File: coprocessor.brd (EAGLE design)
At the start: 27.9 x 64.8 mm, 52 parts, among them IC1 MEGA32U2, U1 TPS61090RSAR, U3 V_REG_LDOSMD2, U4 AZV321

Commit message: Added some aesthetics
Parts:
- FRAME2: value FRAME-LETTER -> Matthew Carlson
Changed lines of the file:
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@@
 </plain>
 <attributes>
+<attribute name="DESIGNER" value="Matthew Carlson"/>
 </attributes>
 <variantdefs>
@@
 <element name="LED2" library="adafruit" package="CHIPLED_0603" value="CHG" x="31.75" y="43.18"/>
 <element name="THERM" library="SparkFun-Resistors" package="0603-RES" value="16k" x="15.24" y="2.54"/>
-<element name="FRAME2" library="SparkFun-Aesthetics" package="CREATIVE_COMMONS" value="FRAME-LETTER" x="17.78" y="-10.16"/>
+<element name="FRAME2" library="SparkFun-Aesthetics" package="CREATIVE_COMMONS" value="Matthew Carlson" x="17.78" y="-10.16"/>
 <element name="U$4" library="custom" package="LOGO_1INCH" value="" x="35.56" y="2.54" rot="R90"/>
 </elements>

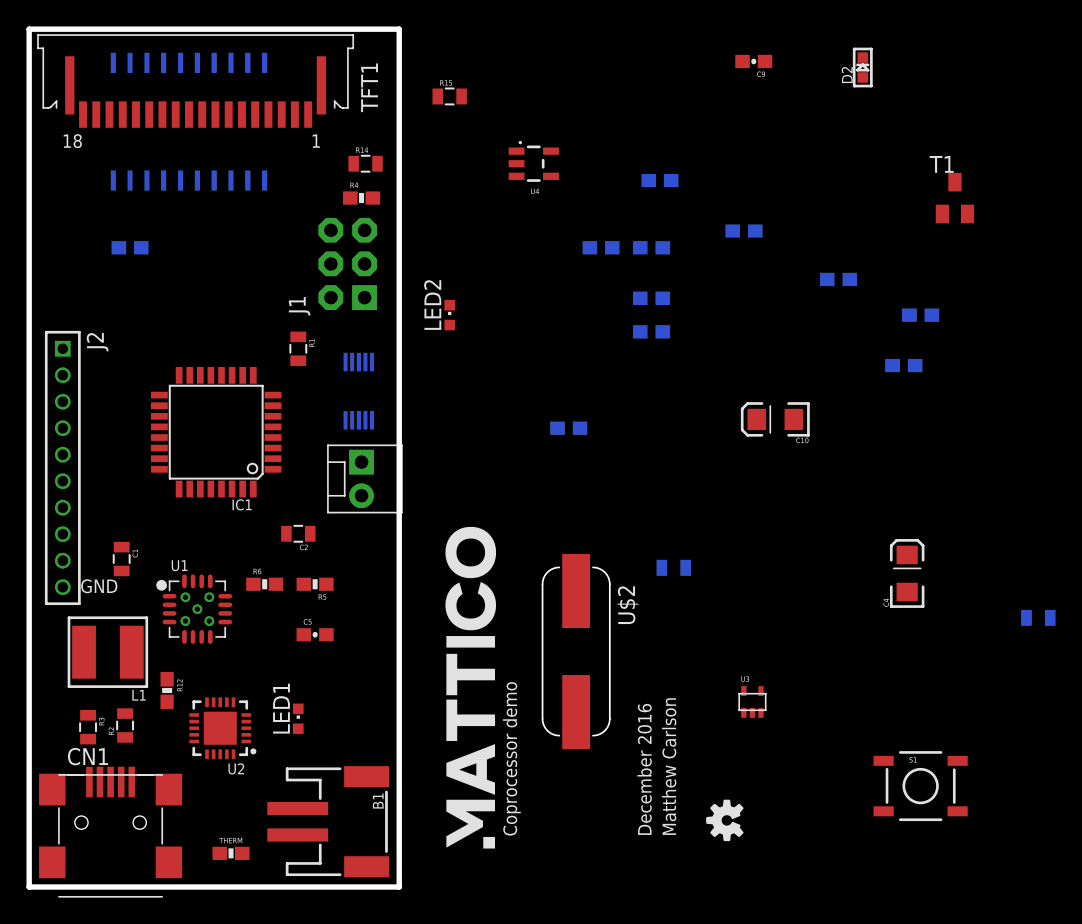
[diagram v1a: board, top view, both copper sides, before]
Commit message: final schematic for revision 2
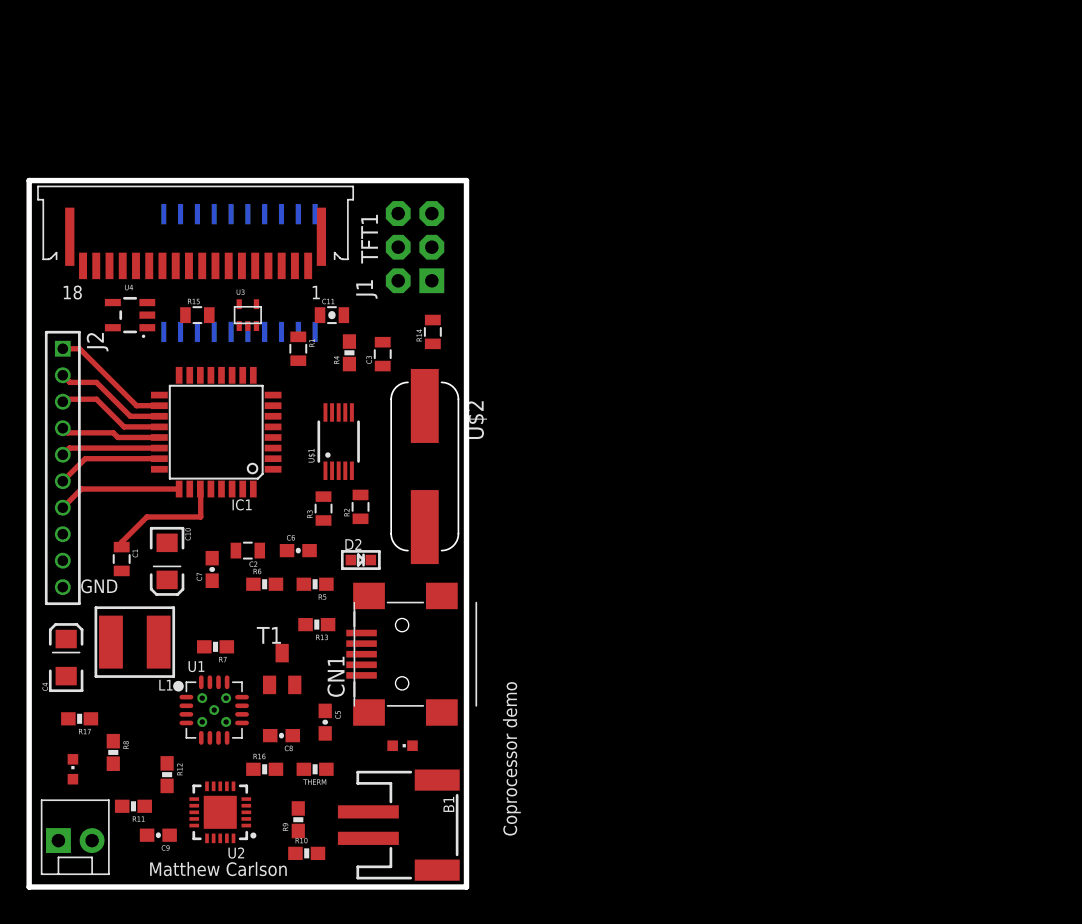
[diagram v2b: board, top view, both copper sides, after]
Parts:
- removed FRAME2: Matthew Carlson, SparkFun-Aesthetics:CREATIVE_COMMONS
- removed S1: RESET, SparkFun-Electromechanical:TACTILE-SWITCH-SMD
- moved C9 73.7 mm to (9.75, 3.91)
- moved R17 70.4 mm to (3.81, 12.7), flipped to the top, turned to 180 degrees
- moved C4 63.8 mm to (2.79, 17.3)
- moved T1 62.0 mm to (19.1, 16.5)
- moved C11 58.0 mm to (22.9, 43.2), flipped to the top
- moved R10 57.4 mm to (21.0, 2.54), flipped to the top
- moved R16 57.1 mm to (17.8, 8.89), flipped to the top
- moved R8 53.2 mm to (6.35, 10.2), flipped to the top, turned to 270 degrees
- moved D2 53.1 mm to (25.0, 24.7), turned to 270 degrees
- moved R11 53.0 mm to (7.87, 6.10), flipped to the top
- moved C7 52.1 mm to (13.8, 24.0), flipped to the top, turned to 90 degrees
- moved R9 48.9 mm to (20.3, 5.08), flipped to the top, turned to 90 degrees
- moved U3 48.0 mm to (16.5, 43.2)
- moved C10 47.2 mm to (10.4, 24.6), turned to 270 degrees
- moved C8 46.2 mm to (19.1, 11.4), flipped to the top, turned to 180 degrees
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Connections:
- new net MCU_CS: IC1.9, U$3.P$2
- new net MCU_MISO: IC1.17
- new net MCU_MOSI: IC1.16, U$3.P$6
- new net MCU_RS: IC1.8, U$3.P$8
- new net MCU_SCK: IC1.15, U$3.P$4
- new net N$28: IC1.22, J2.5
- new net N$29: IC1.23, J2.6
- new net N$30: IC1.25, J2.7
- net GND: now also J2.10; no longer S1.1
- net MISO: no longer IC1.17
- net MOSI: no longer IC1.16
- net N$25: now also IC1.19, J2.2; no longer U$3.P$4
- net N$26: now also IC1.20, J2.3; no longer U$3.P$6
- net N$27: now also IC1.21, J2.4; no longer U$3.P$8
- net N$5: now also IC1.18, J2.1; no longer U$3.P$2
- net RESET: now also J2.8; no longer S1.3
- net SCK: no longer IC1.15
- net TFT_CS: no longer IC1.9
- net TFT_RS: no longer IC1.8
- net VCC: now also J2.9
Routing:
- net N$30: track 0.00 -> 9.37 mm
- net N$7: track 0.00 -> 9.24 mm
- net N$5: track 0.00 -> 9.07 mm
- net N$25: track 0.00 -> 8.57 mm
- net N$26: track 0.00 -> 8.23 mm
- net N$29: track 0.00 -> 7.99 mm
- net N$27: track 0.00 -> 7.58 mm
- net N$28: track 0.00 -> 7.50 mm
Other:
- board size 27.9 x 64.8 mm -> 33 x 53.3 mm
- board text added: "January 2017"
- board text removed: "December 2016"

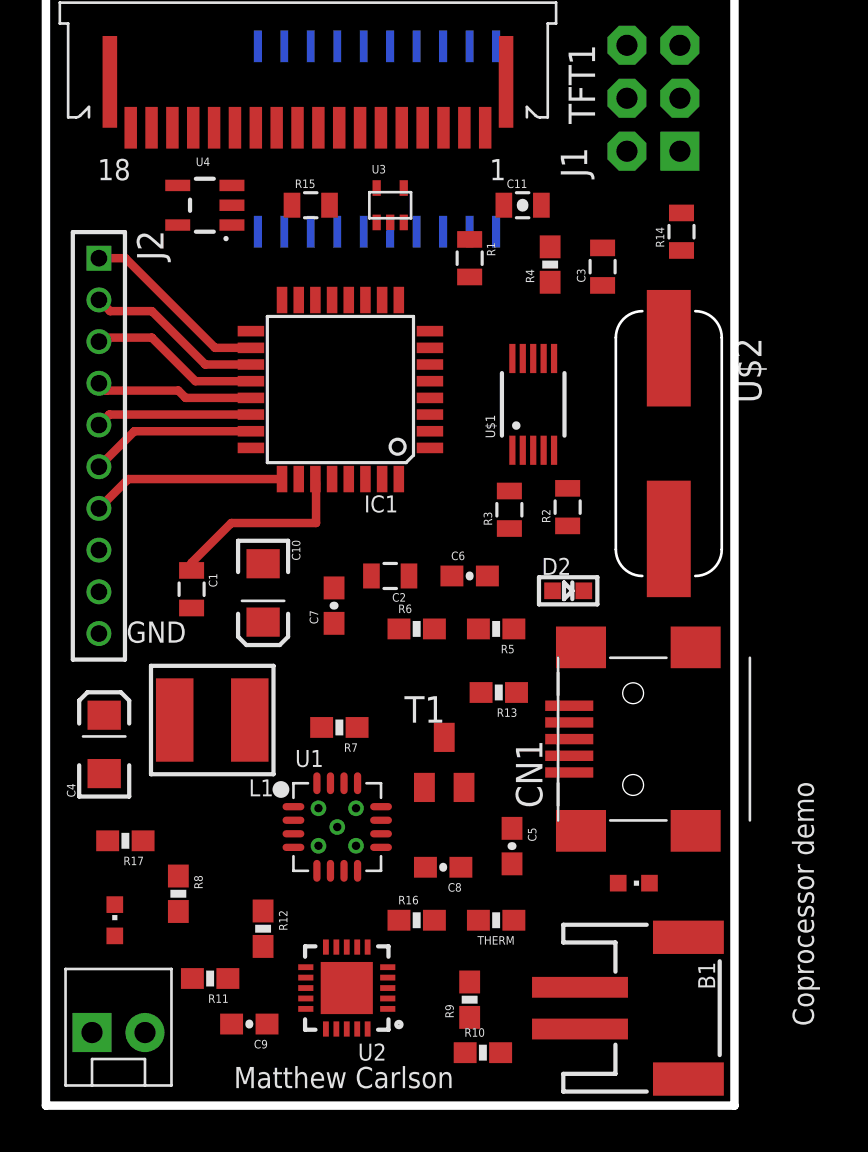
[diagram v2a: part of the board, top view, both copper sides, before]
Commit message: fixed a minor bug on the Bus switch PB2->PC2
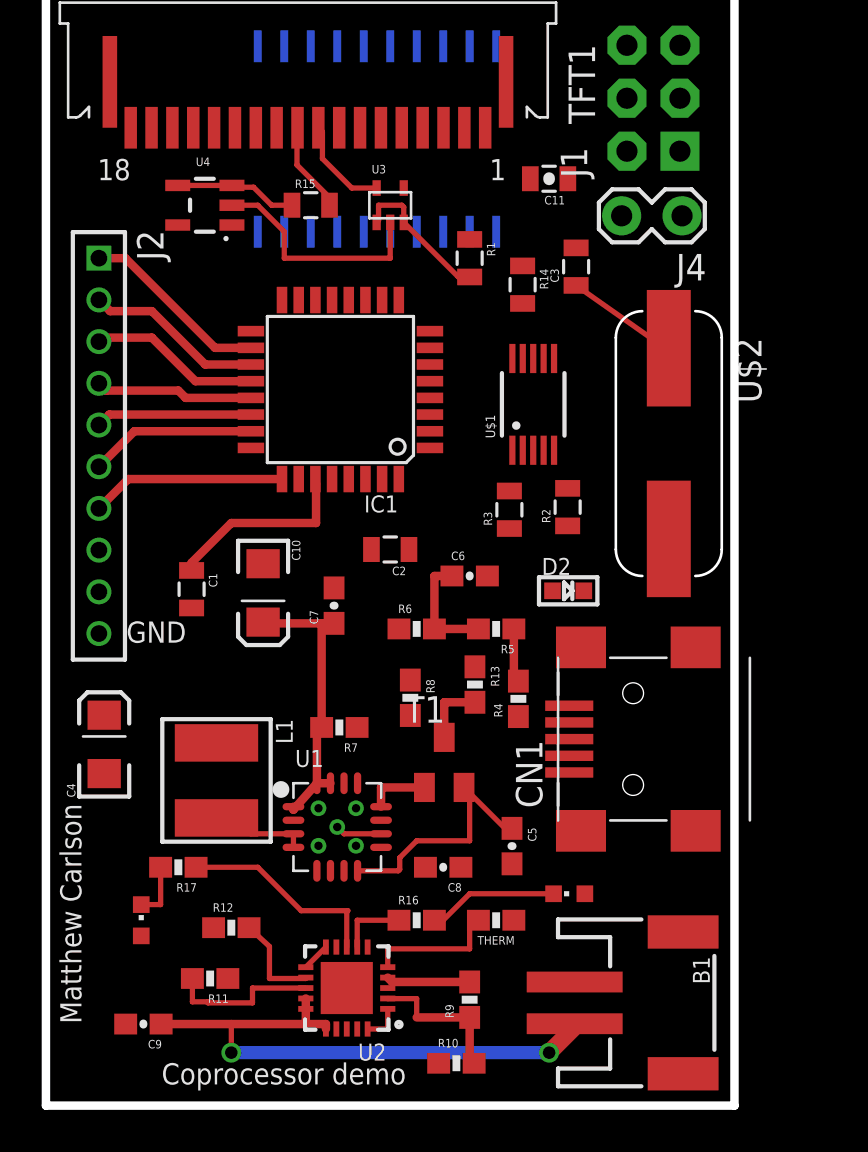
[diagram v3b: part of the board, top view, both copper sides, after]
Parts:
- J4: device SparkFun-Connectors:MOLEX-1X2 -> SparkFun-Connectors:1X02_LOCK
- moved J4 48.2 mm to (30.3, 42.7), turned to 180 degrees
- moved R4 20.9 mm to (22.7, 19.5)
- moved R8 14.6 mm to (17.5, 19.6)
- moved R14 8.03 mm to (22.9, 39.4), turned to 270 degrees
- moved C9 5.08 mm to (4.67, 3.91)
- moved LED1 3.14 mm to (25.1, 10.2), turned to 90 degrees
- moved L1 2.90 mm to (8.18, 15.6), turned to 270 degrees
- moved R17 2.84 mm to (6.35, 11.4)
- moved C11 1.80 mm to (24.1, 44.5), turned to 180 degrees
- moved R12 1.52 mm to (8.89, 8.53), turned to 0 degrees
- moved R10 1.37 mm to (19.7, 2.03)
- moved C2 1.27 mm to (16.5, 26.7)
- moved LED2 1.27 mm to (4.57, 8.89)
- moved C3 1.27 mm to (25.4, 40.2)
- moved LOGO1 1.27 mm to (28.6, 39.3)
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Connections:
- removed net PB2: R14.1, U$3.P$1
- new net PC2: IC1.5, R14.1, U$3.P$1
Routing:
- net N$8: track 0.00 -> 27.9 mm, vias 0 -> 2
- net V_BATT: track 0.00 -> 19.5 mm
- net 5V: track 0.00 -> 14.9 mm
- net GND: track 0.00 -> 14.7 mm
- net N$21: track 0.00 -> 9.91 mm
- net VCC: track 0.00 -> 7.43 mm
- net N$12: track 0.00 -> 7.32 mm
- net N$1: track 0.00 -> 7.25 mm
- net N$24: track 0.00 -> 6.60 mm
- net N$22: track 0.00 -> 6.24 mm
- net N$20: track 0.00 -> 5.87 mm
- net N$10: track 0.00 -> 5.40 mm
- net 2.8V: track 0.00 -> 4.75 mm
- net N$14: track 0.00 -> 4.65 mm
- net N$19: track 0.00 -> 4.37 mm
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
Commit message: addeda bill of materials
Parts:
- moved J4 2.71 mm to (28.1, 41.1), turned to 0 degrees
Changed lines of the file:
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@@
 <element name="C4" library="SparkFun-Capacitors" package="EIA3216" value="10uF" x="2.794" y="17.3228" rot="R90"/>
 <element name="U$1" library="custom" package="10-MSOP" value="MCP48FEB01-E/UN" x="23.368" y="33.6296" rot="R90"/>
-<element name="J4" library="SparkFun-Connectors" package="1X02_LOCK" value="" x="30.3276" y="42.672" rot="R180"/>
+<element name="J4" library="SparkFun-Connectors" package="1X02_LOCK" value="" x="28.0924" y="41.148"/>
 <element name="U$2" library="custom" package="HC49/US" value="16MHZ" x="29.8704" y="31.75" rot="R270"/>
 <element name="R4" library="SparkFun-Resistors" package="0603-RES" value="340k" x="22.6568" y="19.5072" rot="R90">
@@
 <contactref element="U$1" pad="4"/>
 <contactref element="J4" pad="1"/>
-<wire x1="23.868" y1="31.4296" x2="30.5054" y2="42.672" width="0" layer="19" extent="1-1"/>
+<wire x1="23.868" y1="31.4296" x2="27.9146" y2="41.148" width="0" layer="19" extent="1-1"/>
 </signal>
 <signal name="DATA-">

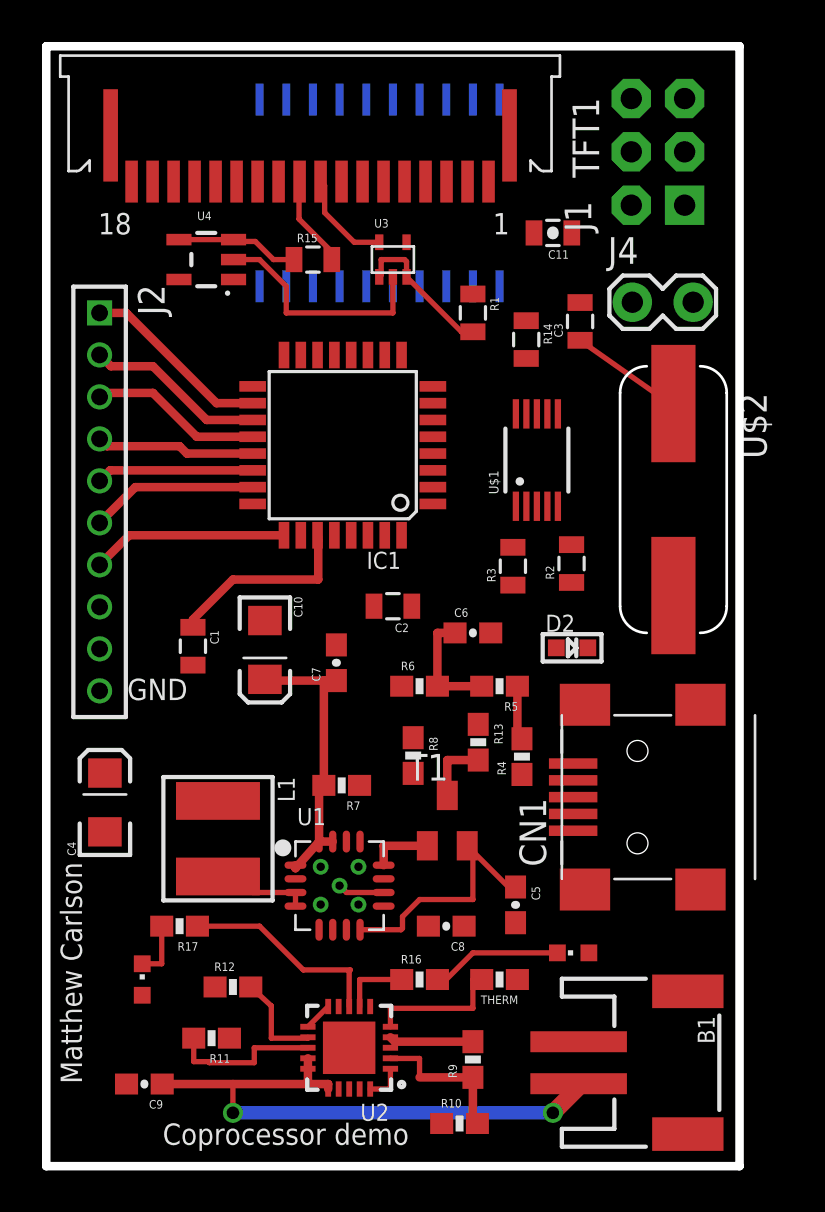
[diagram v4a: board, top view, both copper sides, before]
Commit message: finished routing the coprocessor board
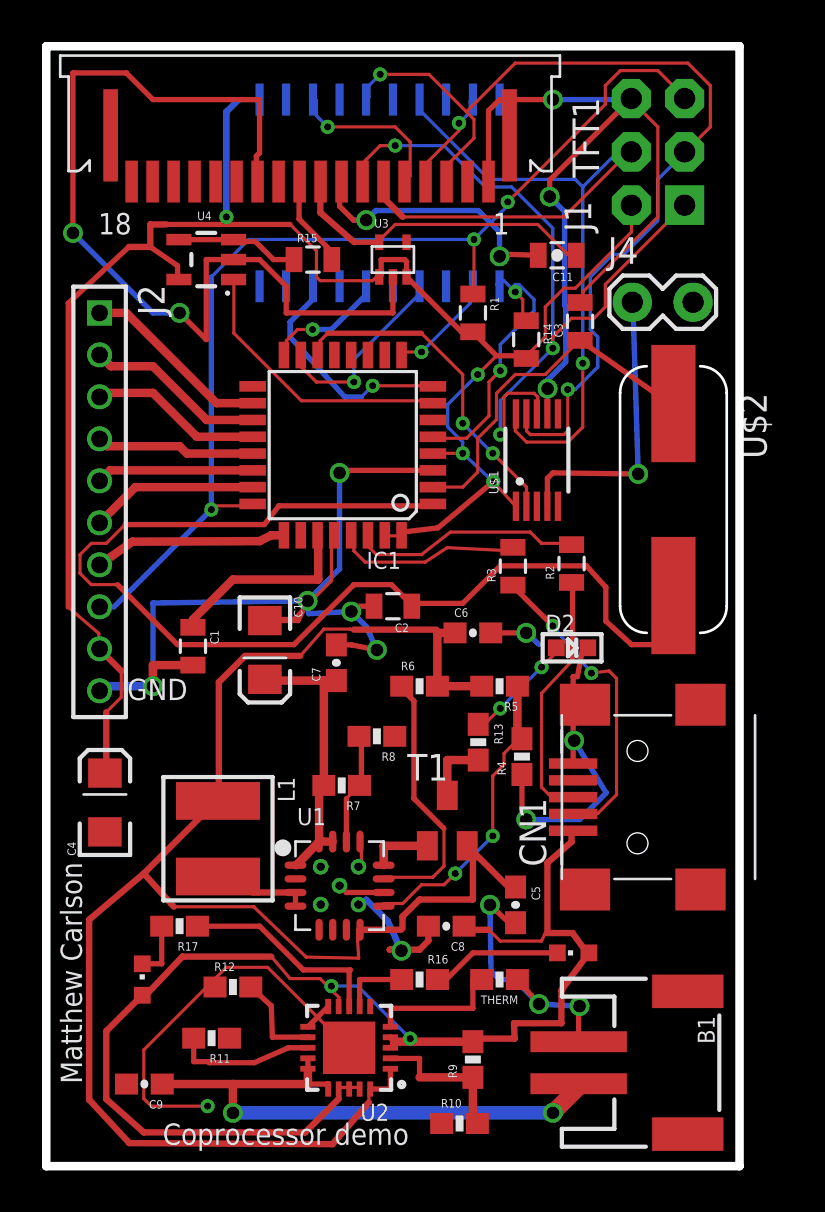
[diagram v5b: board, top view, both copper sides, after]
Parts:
- moved U$4 12.0 mm to (26.0, 0.76)
- moved LOGO1 11.4 mm to (28.6, 27.9)
- moved R8 1.95 mm to (15.7, 20.5), turned to 180 degrees
- moved C11 1.09 mm to (24.3, 43.4)
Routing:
- net GND: track 14.7 -> 203.6 mm, vias 0 -> 20
- net VCC: track 7.43 -> 89.3 mm, vias 0 -> 4
- net V_BATT: track 19.5 -> 82.9 mm
- net V_USB: track 4.01 -> 62.0 mm, vias 0 -> 2
- net N$9: track 0.00 -> 55.2 mm
- net RESET: track 0.00 -> 50.9 mm, vias 0 -> 3
- net SCK: track 0.00 -> 46.3 mm, vias 0 -> 2
- net MOSI: track 0.00 -> 43.0 mm, vias 0 -> 1
- net MISO: track 0.00 -> 37.3 mm, vias 0 -> 3
- net PB0: track 0.00 -> 16.0 mm, vias 0 -> 2
- net DATA-: track 0.00 -> 15.0 mm, vias 0 -> 2
- net PC2: track 0.00 -> 14.0 mm, vias 0 -> 2
- net DAC_VOUT: track 0.00 -> 14.0 mm, vias 0 -> 1
- net TFT_LED: track 0.00 -> 13.5 mm
- net N$4: track 0.00 -> 12.5 mm
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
